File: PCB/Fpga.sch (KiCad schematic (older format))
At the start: 4 parts

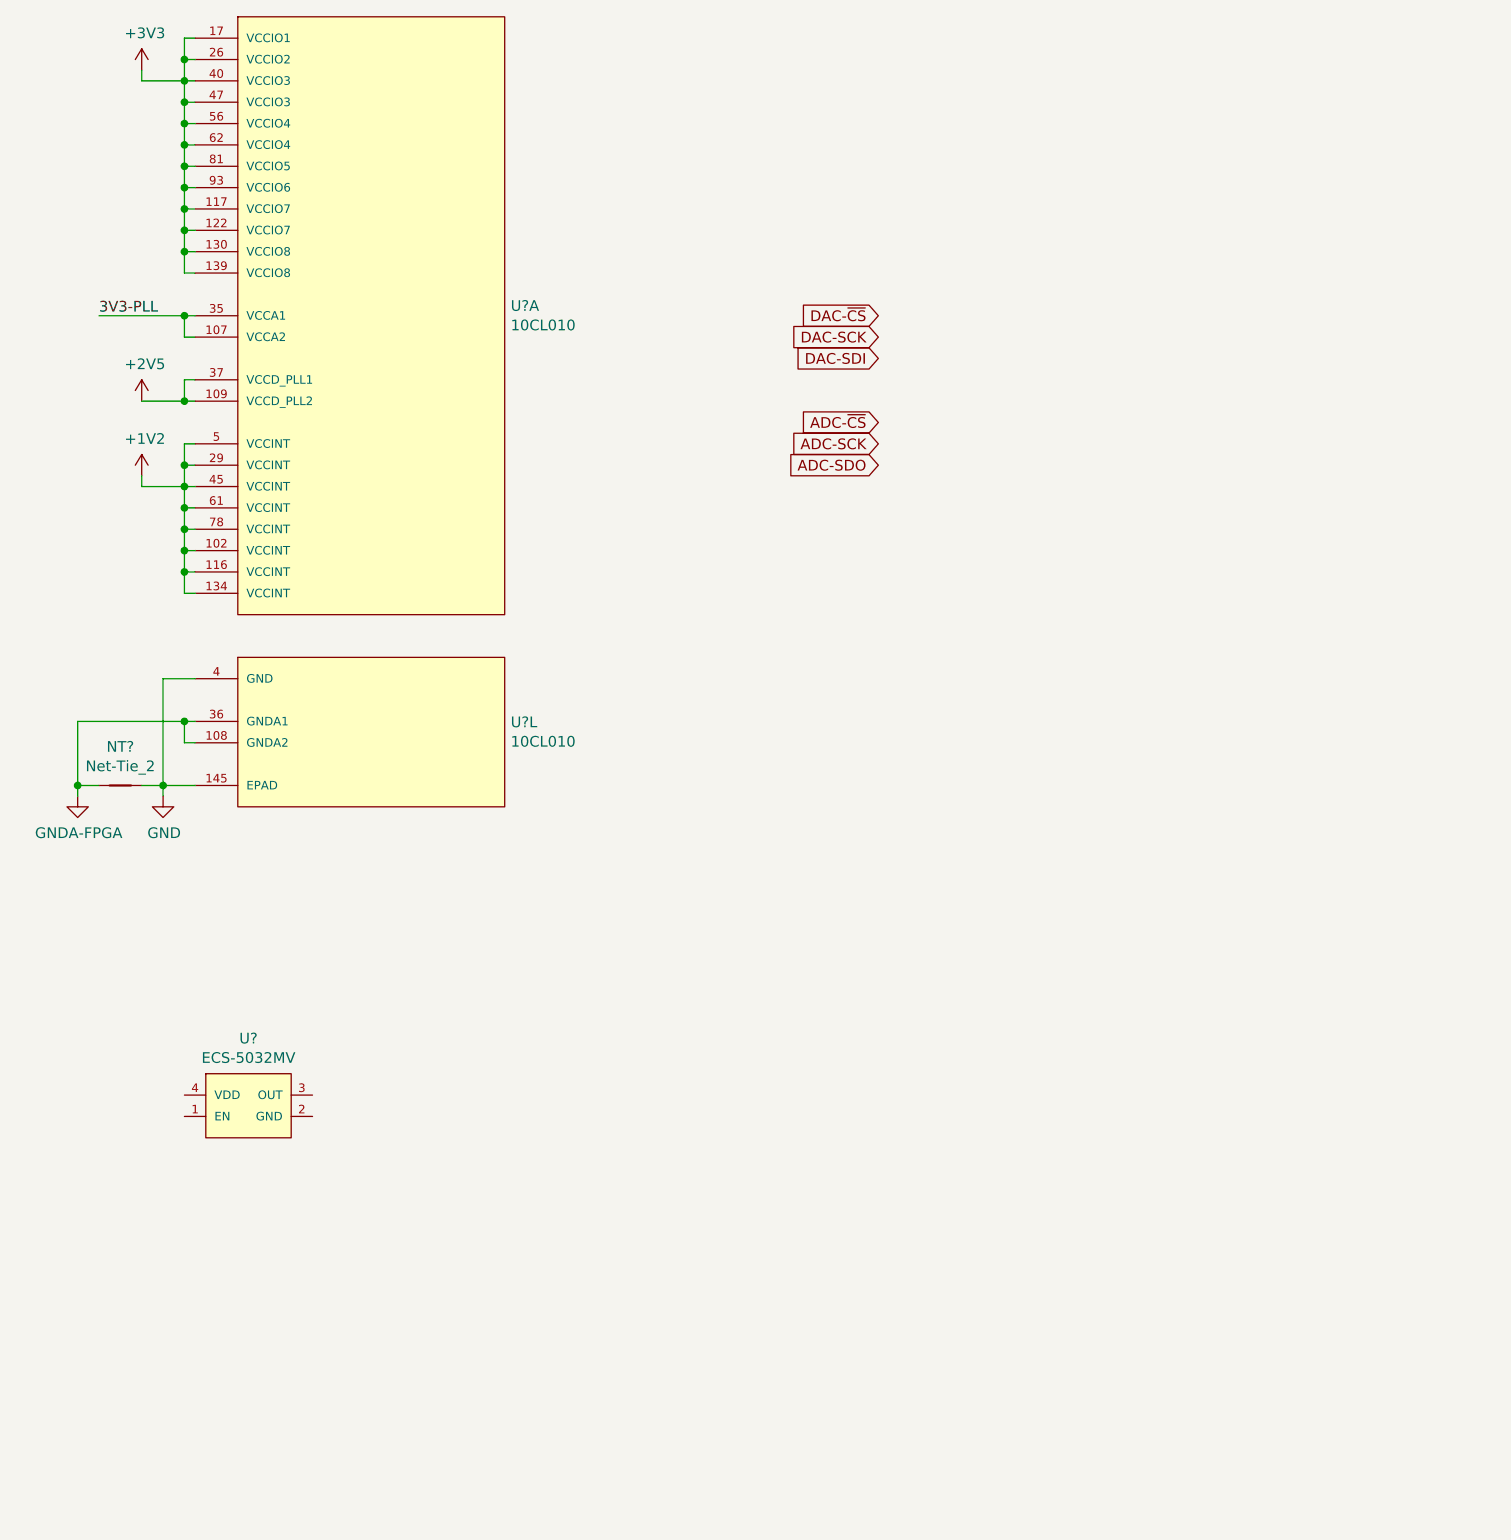
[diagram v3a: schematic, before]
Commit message: Begin adding FPGA connections for JTAG
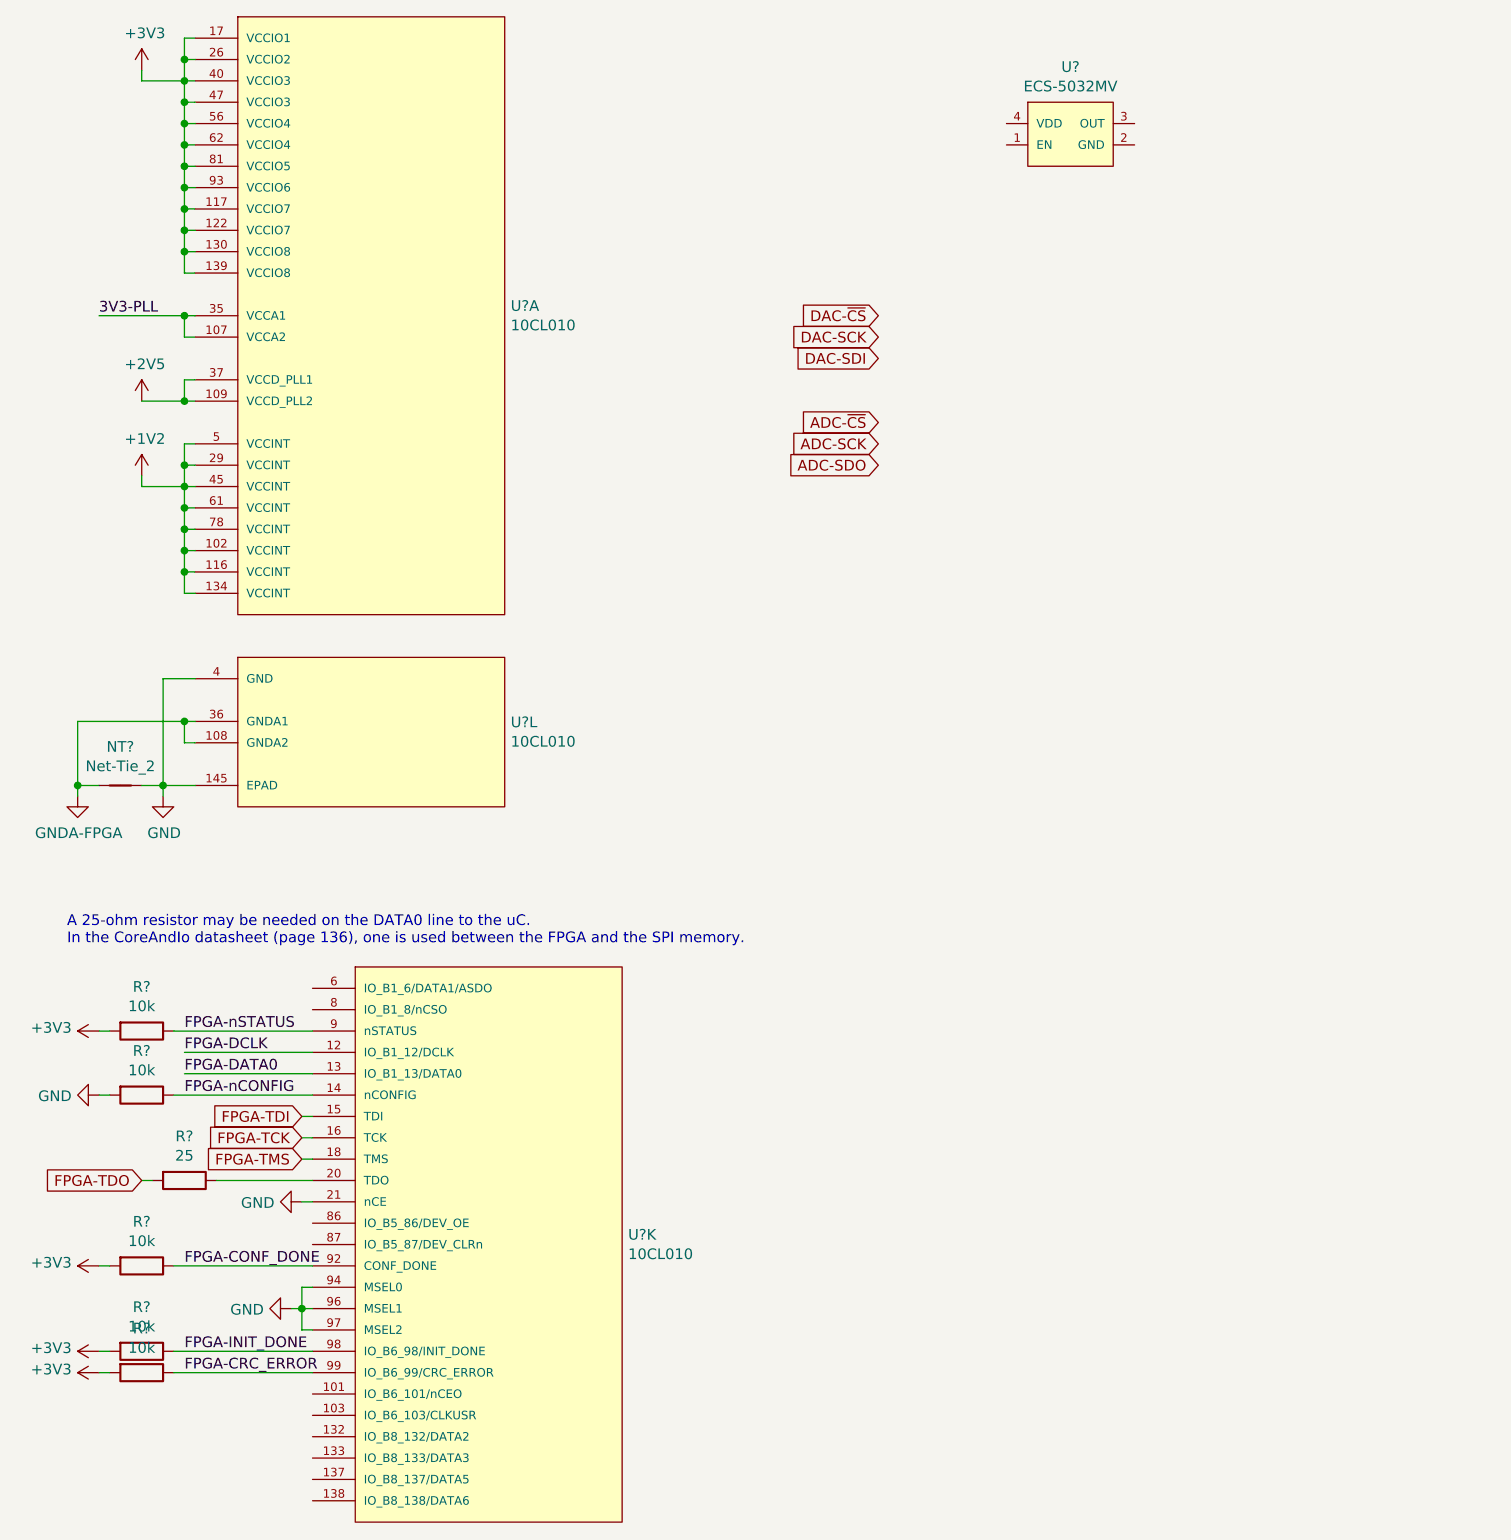
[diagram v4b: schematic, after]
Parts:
- added R? (x5): 10k, symbol Device:R
- added R?: 25, symbol Device:R
- added U?: 10CL010, Parts:EQFP144-PAD, symbol Parts:10CL010
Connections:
- net +3V3: now also R?.2, R?.2, R?.2, R?.2
- net GND: now also R?.2, U?.21 (nCE), U?.94 (MSEL0), U?.96 (MSEL1), U?.97 (MSEL2)
- new net: R?.1, U?.20 (TDO)
- new net FPGA-CONF_DONE: R?.1, U?.92 (CONF_DONE)
- new net FPGA-CRC_ERROR: R?.1, U?.99 (IO_B6_99/CRC_ERROR)
- new net FPGA-DATA0: U?.13 (IO_B1_13/DATA0)
- new net FPGA-DCLK: U?.12 (IO_B1_12/DCLK)
- new net FPGA-INIT_DONE: R?.1, U?.98 (IO_B6_98/INIT_DONE)
- new net FPGA-TCK: U?.16 (TCK)
- new net FPGA-TDI: U?.15 (TDI)
- new net FPGA-TDO: R?.2
- new net FPGA-TMS: U?.18 (TMS)
- new net FPGA-nCONFIG: R?.1, U?.14 (nCONFIG)
- new net FPGA-nSTATUS: R?.1, U?.9 (nSTATUS)
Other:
- note added: "A 25-ohm resistor may be needed on the DATA0 line to the uC.\nIn the CoreAndIo datasheet (page 136), one is used between the FPGA and the SPI memory."
- moved on the sheet: U?
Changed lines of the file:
@@
 L Parts:ECS-5032MV U?
 U 1 1 5DD22CF7
-P 1600 5700
-F 0 "U?" H 1600 6015 50  0000 C CNN
-F 1 "ECS-5032MV" H 1600 5924 50  0000 C CNN
-F 2 "Parts:ECS-5032MV" H 1600 5400 50  0001 C CNN
-F 3 "https://ecsxtal.com/ecs-5032mv" H 1600 5300 50  0001 C CNN
-	1    1600 5700
+P 5450 1150
+F 0 "U?" H 5450 1465 50  0000 C CNN
+F 1 "ECS-5032MV" H 5450 1374 50  0000 C CNN
+F 2 "Parts:ECS-5032MV" H 5450 850 50  0001 C CNN
+F 3 "https://ecsxtal.com/ecs-5032mv" H 5450 750 50  0001 C CNN
+	1    5450 1150
 	1    0    0    -1
 $EndComp
@@
 Text GLabel 4550 2700 0    50   Input ~ 0
 ADC-SDO
+$Comp
+L Parts:10CL010 U?
+U 11 1 5DE8AD4C
+P 2100 5050
+F 0 "U?" H 3378 3796 50  0000 L CNN
+F 1 "10CL010" H 3378 3705 50  0000 L CNN
+F 2 "Parts:EQFP144-PAD" H 2950 5100 50  0001 L BNN
+F 3 "https://www.intel.com/content/www/us/en/programmable/products/fpga/cyclone-series/cyclone-10/cyclone-10-lp/support.html" H 2100 5050 50  0001 C CNN
+	11   2100 5050
+	1    0    0    -1
+$EndComp
+$Comp
+L power:GND #PWR?
+U 1 1 5DE951FF
+P 1800 6650
+F 0 "#PWR?" H 1800 6400 50  0001 C CNN
+F 1 "GND" V 1805 6522 50  0000 R CNN
+F 2 "" H 1800 6650 50  0001 C CNN
+F 3 "" H 1800 6650 50  0001 C CNN
+	1    1800 6650
+	0    1    1    0
+$EndComp
+Wire Wire Line
+	1900 6550 1850 6550
+Wire Wire Line
+	1850 6550 1850 6650
+Wire Wire Line
+	1850 6650 1900 6650
+Wire Wire Line
+	1900 6750 1850 6750
+Wire Wire Line
+	1850 6750 1850 6650
+Connection ~ 1850 6650
+Text GLabel 1850 5750 0    50   Input ~ 0
+FPGA-TDI
+Text GLabel 1850 5850 0    50   Input ~ 0
+FPGA-TCK
+Text GLabel 1850 5950 0    50   Input ~ 0
+FPGA-TMS
+Text GLabel 1100 6050 0    50   Input ~ 0
+FPGA-TDO
+Wire Wire Line
+	1850 5750 1900 5750
+Wire Wire Line
+	1900 5850 1850 5850
+Wire Wire Line
+	1850 5950 1900 5950
+Wire Wire Line
+	1900 6050 1450 6050
+$Comp
+L Device:R R?
+U 1 1 5DEDA0A1
+P 1100 5350
+F 0 "R?" V 893 5350 50  0000 C CNN
+F 1 "10k" V 984 5350 50  0000 C CNN
+F 2 "" V 1030 5350 50  0001 C CNN
+F 3 "~" H 1100 5350 50  0001 C CNN
+	1    1100 5350
+	0    1    1    0
+$EndComp
+$Comp
+L power:+3V3 #PWR?
+U 1 1 5DEE2282
+P 900 5350
+F 0 "#PWR?" H 900 5200 50  0001 C CNN
+F 1 "+3V3" V 915 5478 50  0000 L CNN
+F 2 "" H 900 5350 50  0001 C CNN
+F 3 "" H 900 5350 50  0001 C CNN
+	1    900  5350
+	0    -1   -1   0
+$EndComp
+$Comp
+L Device:R R?
+U 1 1 5DEEE88D
+P 1100 6450
+F 0 "R?" V 893 6450 50  0000 C CNN
+F 1 "10k" V 984 6450 50  0000 C CNN
+F 2 "" V 1030 6450 50  0001 C CNN
+F 3 "~" H 1100 6450 50  0001 C CNN
+	1    1100 6450
+	0    1    1    0
+$EndComp
+$Comp
+L power:+3V3 #PWR?
+U 1 1 5DEF4015
+P 900 6450
+F 0 "#PWR?" H 900 6300 50  0001 C CNN
+F 1 "+3V3" V 915 6578 50  0000 L CNN
+F 2 "" H 900 6450 50  0001 C CNN
+F 3 "" H 900 6450 50  0001 C CNN
+	1    900  6450
+	0    -1   -1   0
+$EndComp
+$Comp
+L Device:R R?
+U 1 1 5DEF75FB
+P 1100 5650
+F 0 "R?" V 893 5650 50  0000 C CNN
+F 1 "10k" V 984 5650 50  0000 C CNN
+F 2 "" V 1030 5650 50  0001 C CNN
+F 3 "~" H 1100 5650 50  0001 C CNN
+	1    1100 5650
+	0    1    1    0
+$EndComp
+$Comp
+L power:GND #PWR?
+U 1 1 5DEFD837
+P 900 5650
+F 0 "#PWR?" H 900 5400 50  0001 C CNN
+F 1 "GND" V 905 5522 50  0000 R CNN
+F 2 "" H 900 5650 50  0001 C CNN
+F 3 "" H 900 5650 50  0001 C CNN
+	1    900  5650
+	0    1    1    0
+$EndComp
+$Comp
+L Device:R R?
+U 1 1 5DF01598
+P 1100 6950
+F 0 "R?" V 893 6950 50  0000 C CNN
+F 1 "10k" V 984 6950 50  0000 C CNN
+F 2 "" V 1030 6950 50  0001 C CNN
+F 3 "~" H 1100 6950 50  0001 C CNN
+	1    1100 6950
+	0    1    1    0
+$EndComp
+$Comp
+L power:+3V3 #PWR?
+U 1 1 5DF077A6
+P 900 6950
+F 0 "#PWR?" H 900 6800 50  0001 C CNN
+F 1 "+3V3" V 915 7078 50  0000 L CNN
+F 2 "" H 900 6950 50  0001 C CNN
+F 3 "" H 900 6950 50  0001 C CNN
+	1    900  6950
+	0    -1   -1   0
+$EndComp
+$Comp
+L Device:R R?
+U 1 1 5DF1AD90
+P 1100 6850
+F 0 "R?" V 893 6850 50  0000 C CNN
+F 1 "10k" V 984 6850 50  0000 C CNN
+F 2 "" V 1030 6850 50  0001 C CNN
+F 3 "~" H 1100 6850 50  0001 C CNN
+	1    1100 6850
+	0    1    1    0
+$EndComp
+$Comp
+L power:+3V3 #PWR?
+U 1 1 5DF213C7
+P 900 6850
+F 0 "#PWR?" H 900 6700 50  0001 C CNN
+F 1 "+3V3" V 915 6978 50  0000 L CNN
+F 2 "" H 900 6850 50  0001 C CNN
+F 3 "" H 900 6850 50  0001 C CNN
+	1    900  6850
+	0    -1   -1   0
+$EndComp
+Wire Wire Line
+	1150 6050 1100 6050
+$Comp
+L Device:R R?
+U 1 1 5DF25E87
+P 1300 6050
+F 0 "R?" V 1093 6050 50  0000 C CNN
+F 1 "25" V 1184 6050 50  0000 C CNN
+F 2 "" V 1230 6050 50  0001 C CNN
+F 3 "~" H 1300 6050 50  0001 C CNN
+	1    1300 6050
+	0    1    1    0
+$EndComp
+$Comp
+L power:GND #PWR?
+U 1 1 5DF31864
+P 1850 6150
+F 0 "#PWR?" H 1850 5900 50  0001 C CNN
+F 1 "GND" V 1855 6022 50  0000 R CNN
+F 2 "" H 1850 6150 50  0001 C CNN
+F 3 "" H 1850 6150 50  0001 C CNN
+	1    1850 6150
+	0    1    1    0
+$EndComp
+Wire Wire Line
+	1850 6150 1900 6150
+Wire Wire Line
+	900  5350 950  5350
+Text Label 1300 5350 0    50   ~ 0
+FPGA-nSTATUS
+Wire Wire Line
+	1250 5350 1900 5350
+Text Label 1300 5450 0    50   ~ 0
+FPGA-DCLK
+Text Label 1300 5550 0    50   ~ 0
+FPGA-DATA0
+Wire Wire Line
+	1250 5650 1900 5650
+Wire Wire Line
+	900  5650 950  5650
+Text Label 1300 5650 0    50   ~ 0
+FPGA-nCONFIG
+Wire Wire Line
+	900  6950 950  6950
+Wire Wire Line
+	1250 6950 1900 6950
+Text Label 1300 6950 0    50   ~ 0
+FPGA-CRC_ERROR
+Wire Wire Line
+	1250 6850 1900 6850
+Wire Wire Line
+	900  6850 950  6850
+Wire Wire Line
+	900  6450 950  6450
+Wire Wire Line
+	1250 6450 1900 6450
+Wire Wire Line
+	1800 6650 1850 6650
+Text Label 1300 6850 0    50   ~ 0
+FPGA-INIT_DONE
+Text Label 1300 6450 0    50   ~ 0
+FPGA-CONF_DONE
+Wire Wire Line
+	1300 5450 1900 5450
+Wire Wire Line
+	1300 5550 1900 5550
+Text Notes 750  4950 0    50   ~ 0
+A 25-ohm resistor may be needed on the DATA0 line to the uC.\nIn the CoreAndIo datasheet (page 136), one is used between the FPGA and the SPI memory.
 $EndSCHEMATC

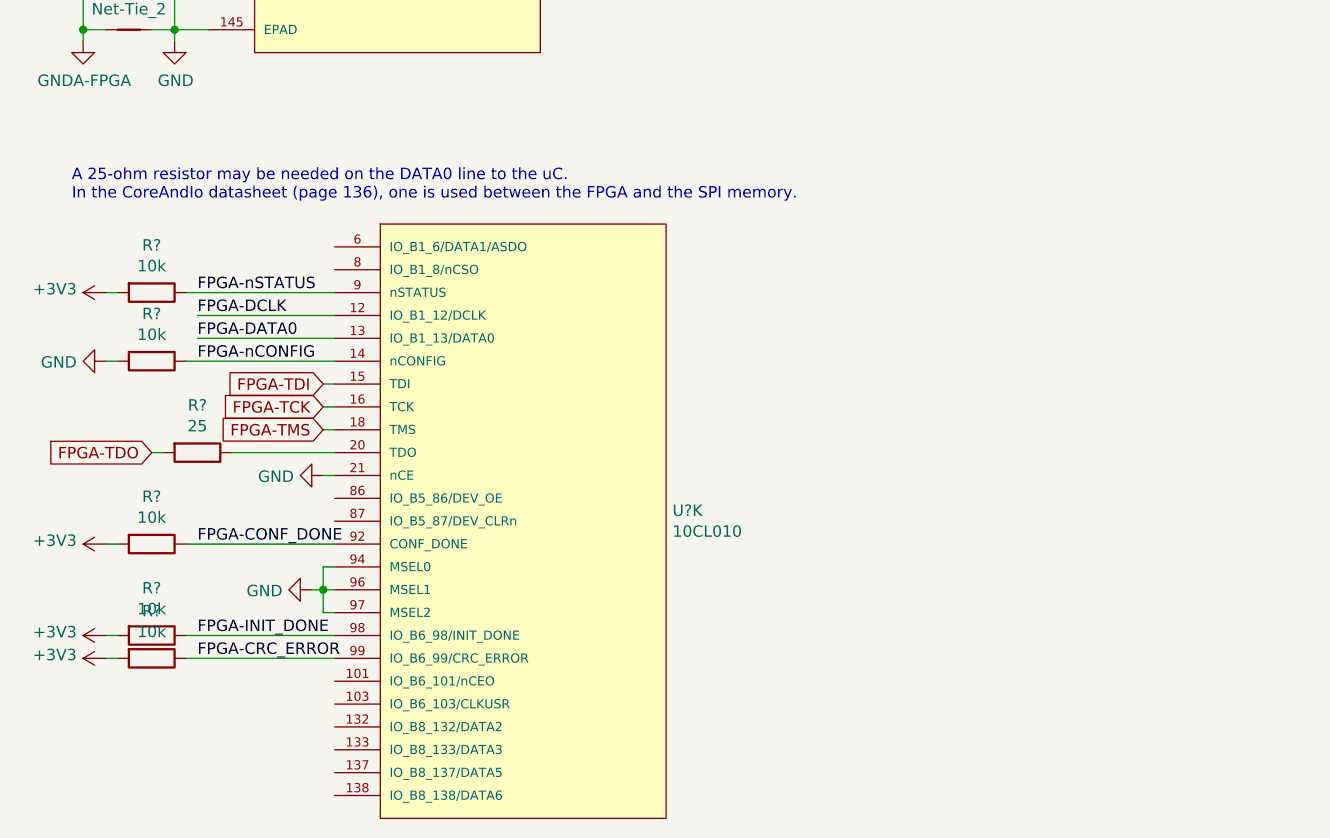
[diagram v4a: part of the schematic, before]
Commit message: Add debug headers for FPGA and microcontroller
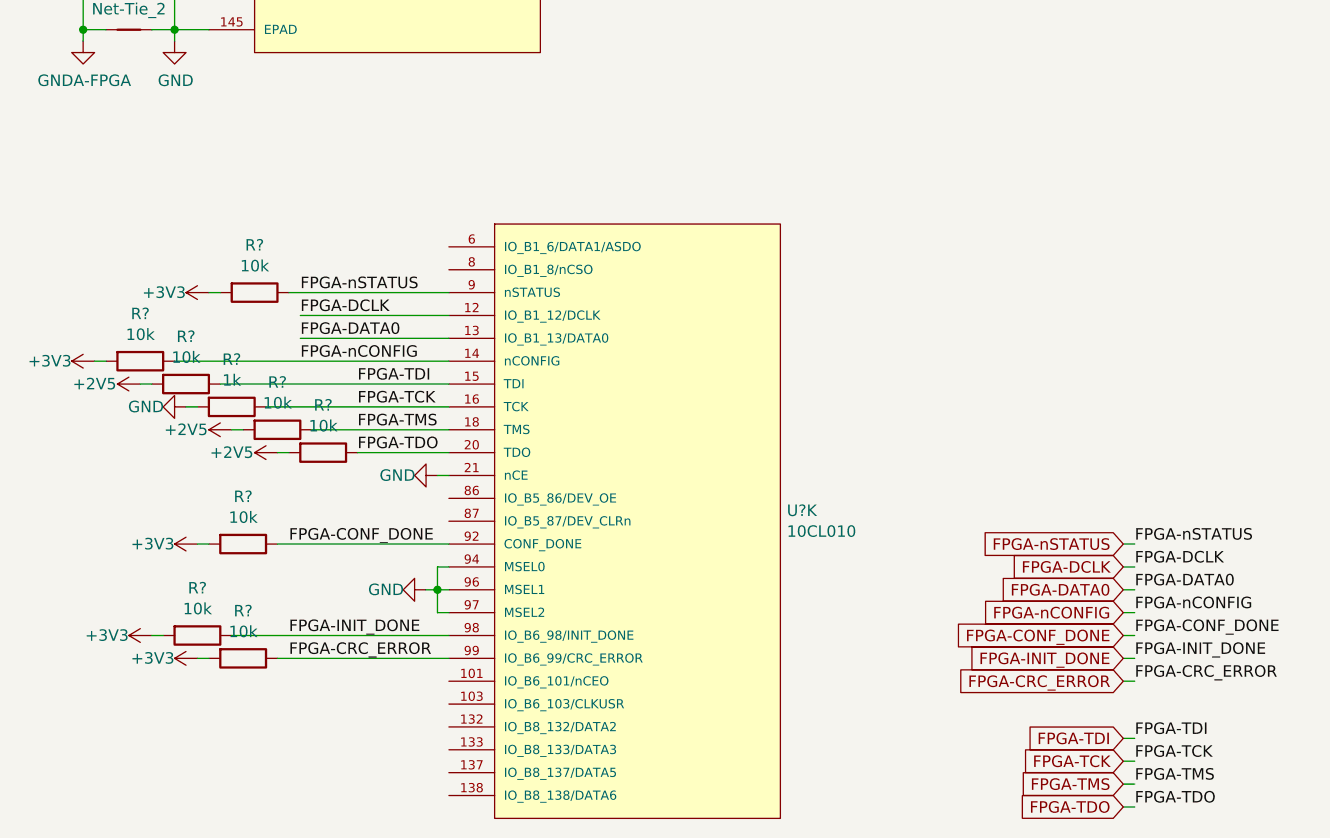
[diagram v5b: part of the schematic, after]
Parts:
- removed R? (x4): 10k, symbol Device:R
- removed R?: 25, symbol Device:R
- added R? (x7): 10k, Resistors_SMD:R_0603_HandSoldering, symbol Device:R
- added R?: 1k, Resistors_SMD:R_0603_HandSoldering, symbol Device:R
- R?: footprint (none) -> Resistors_SMD:R_0603_HandSoldering
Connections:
- net +2V5: now also R?.2, R?.2, R?.2
- net +3V3: now also R?.2, R?.2, R?.2, R?.2
- net FPGA-CONF_DONE: now also R?.1
- net FPGA-CRC_ERROR: now also R?.1
- net FPGA-INIT_DONE: now also R?.1
- net FPGA-TCK: now also R?.1
- net FPGA-TDI: now also R?.1
- net FPGA-TDO: now also U?.20 (TDO), R?.1
- net FPGA-TMS: now also R?.1
- net FPGA-nCONFIG: now also R?.1
- net GND: now also R?.2
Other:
- note removed: "A 25-ohm resistor may be needed on the DATA0 line to the uC.\nIn the CoreAndIo datasheet (page 136), one is used between the FPGA and the SPI memory."
- moved on the sheet: R?, U?K
